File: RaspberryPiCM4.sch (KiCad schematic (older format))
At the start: 12 parts, among them U11 Compute_Module_4_Connectors

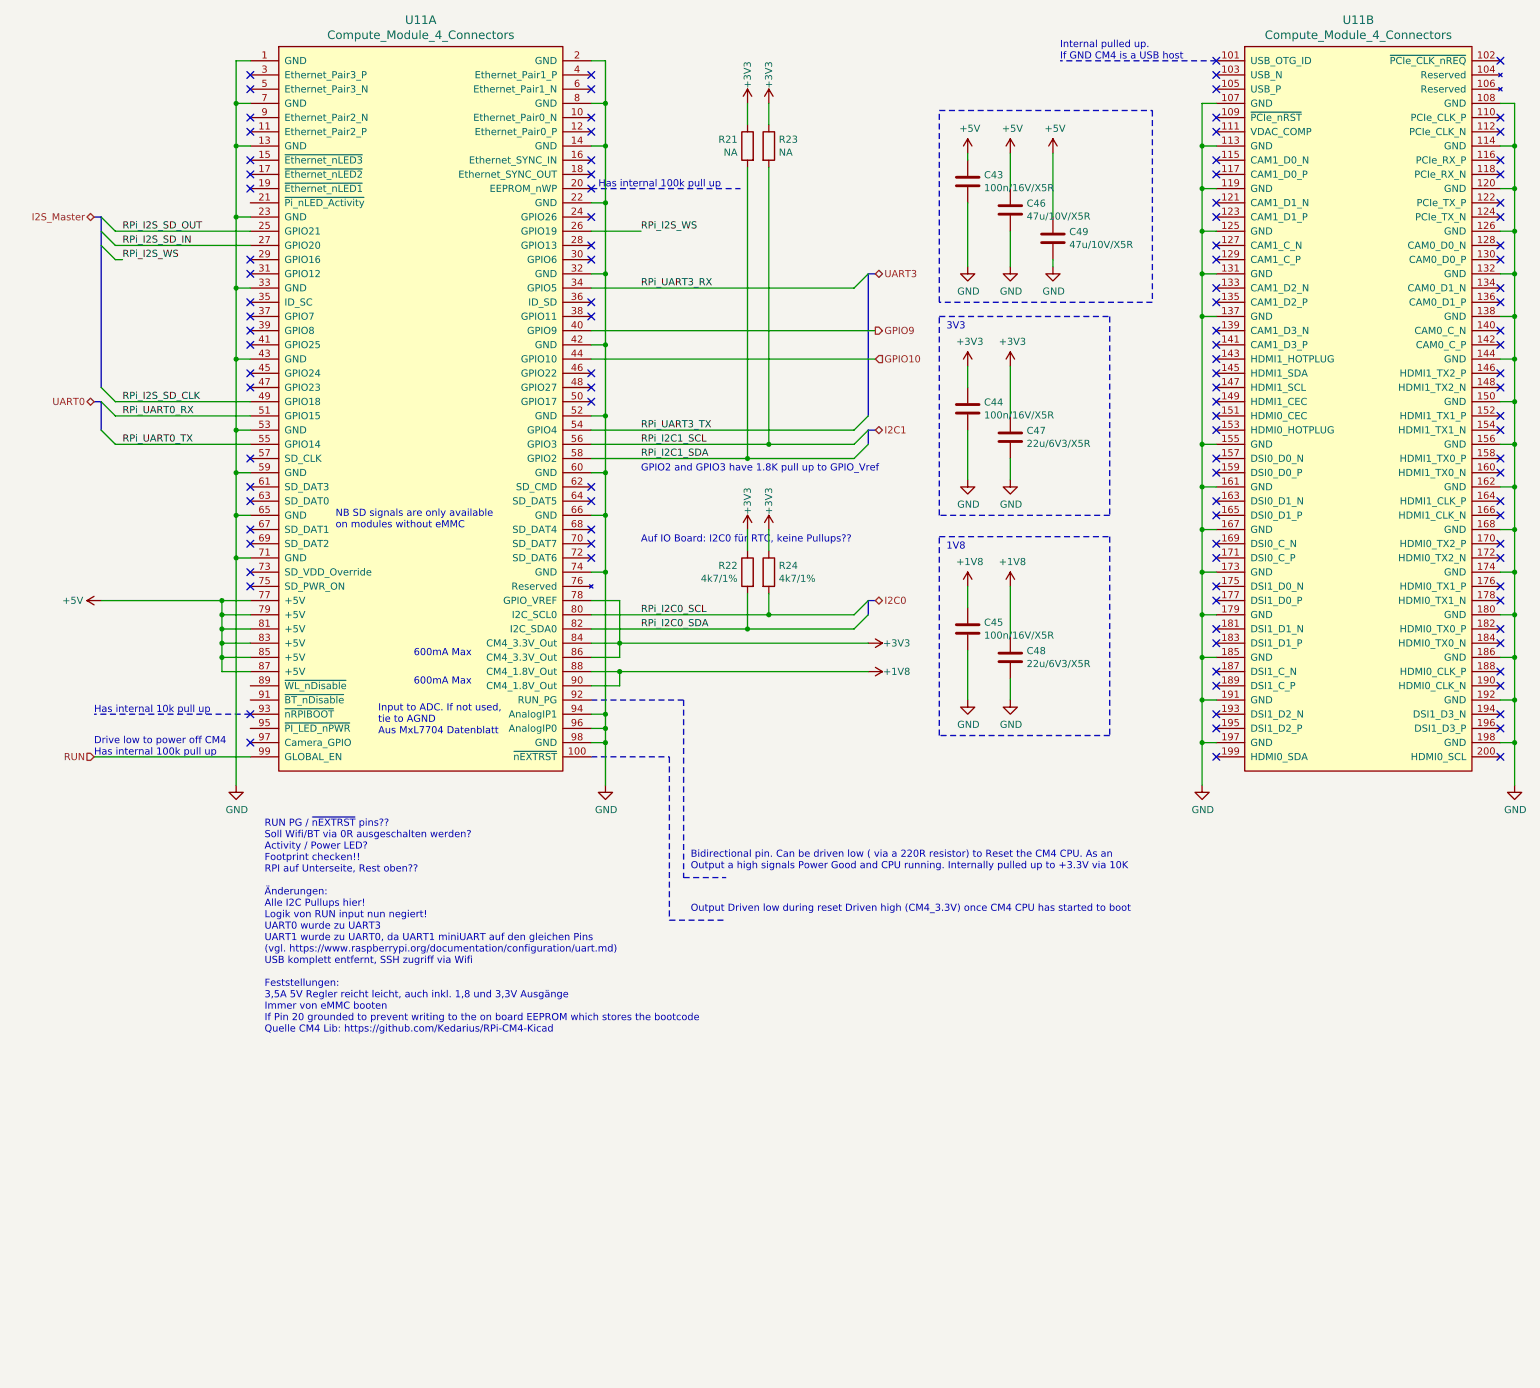
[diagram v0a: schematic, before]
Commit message: - 0R Bruecken hinzugefuegt - viele Detailinfos
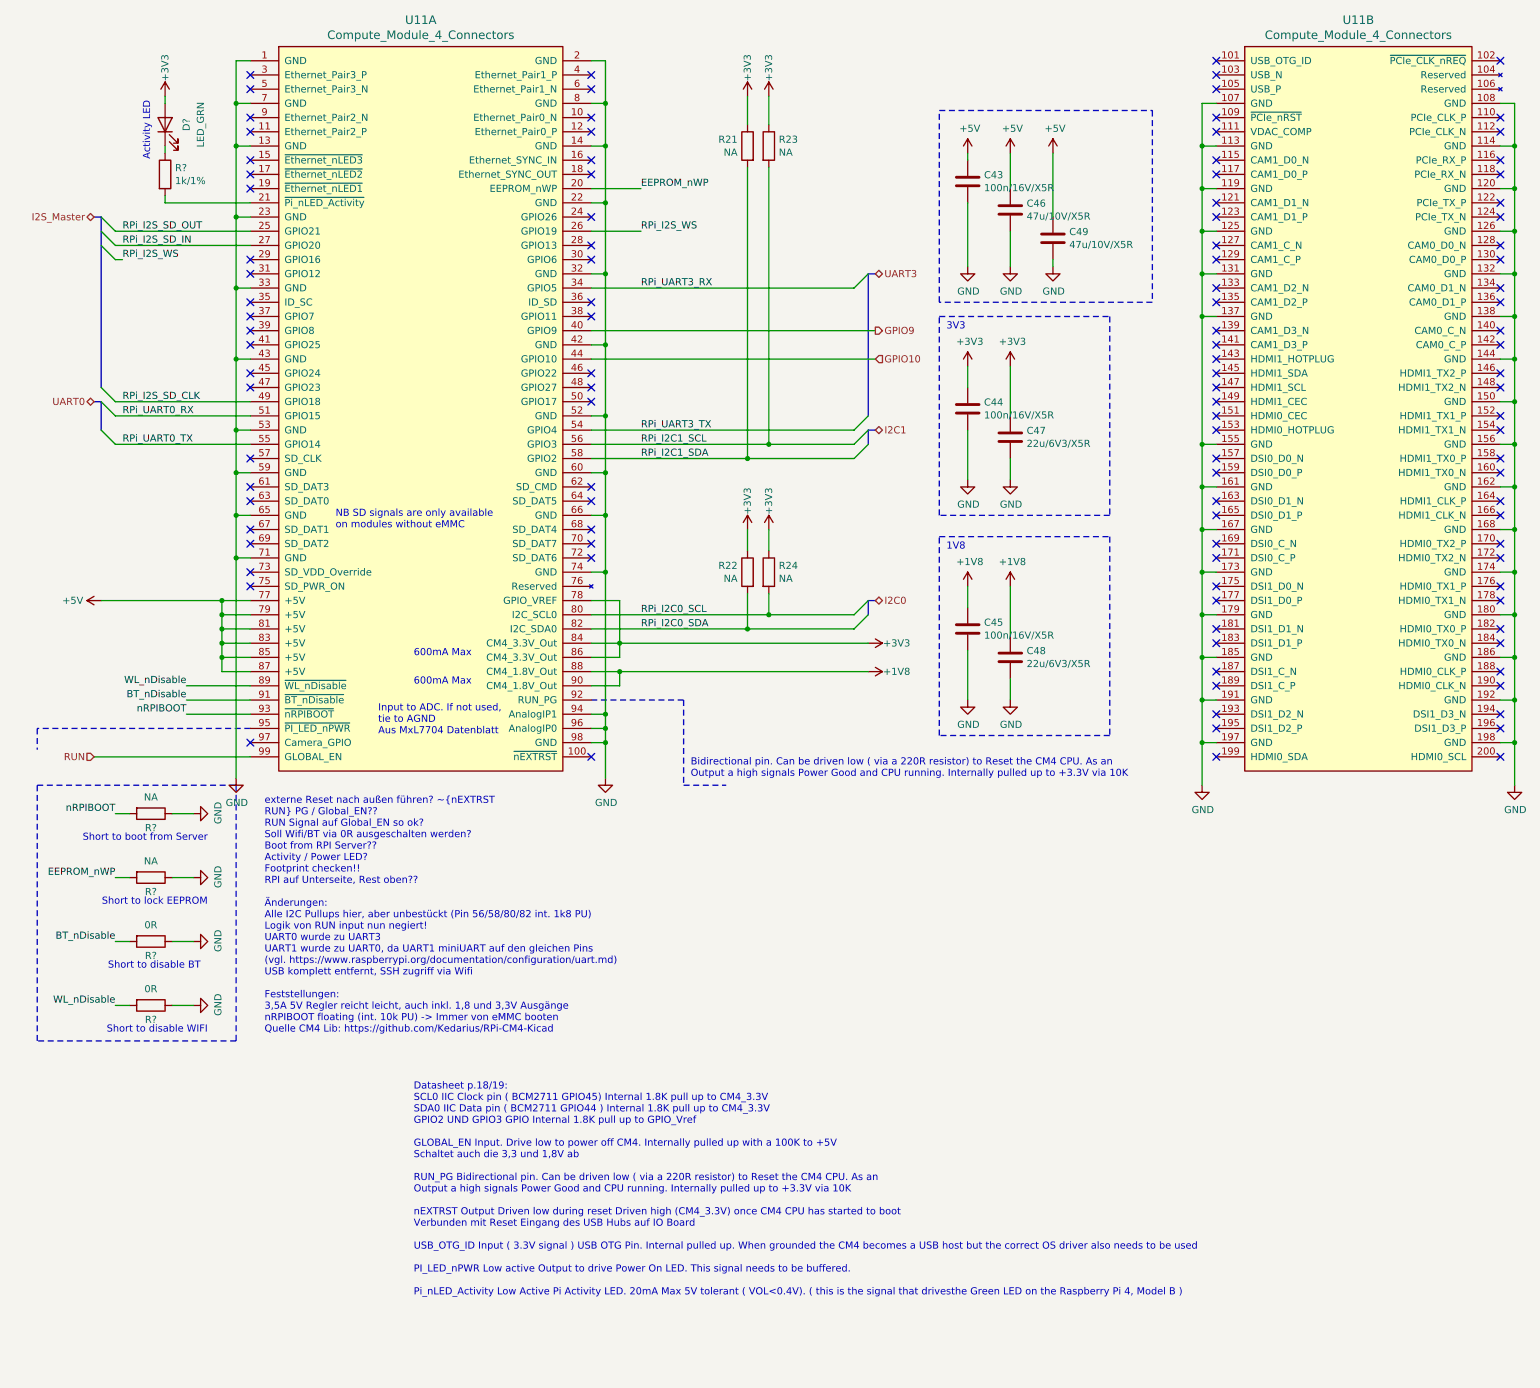
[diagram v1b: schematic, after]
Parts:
- added D?: LED_GRN, LED_SMD:LED_0603_1608Metric, symbol Device:LED
- added R? (x2): NA, Resistor_SMD:R_0402_1005Metric, symbol Device:R
- added R? (x2): 0R, Resistor_SMD:R_0402_1005Metric, symbol Device:R
- added R?: 1k/1%, Resistor_SMD:R_0603_1608Metric, symbol Device:R
- R21, R23: footprint Resistor_SMD:R_0603_1608Metric -> Resistor_SMD:R_0402_1005Metric
- R22, R24: value 4k7/1% -> NA; footprint Resistor_SMD:R_0603_1608Metric -> Resistor_SMD:R_0402_1005Metric
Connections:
- net +3V3: now also D?.2 (A)
- net GND: now also R?.1, R?.1, R?.1, R?.1
- net EEPROM_nWP: now reaches U11.20 (EEPROM_nWP)
- net EEPROM_nWP: now also R?.2
- net at U11.21 (~Pi_nLED_Activity): now also R?.2
- net WL_nDisable: now reaches U11.89 (~WL_nDisable)
- net WL_nDisable: now also R?.2
- net BT_nDisable: now reaches U11.91 (~BT_nDisable)
- net BT_nDisable: now also R?.2
- net nRPIBOOT: now reaches U11.93 (~nRPIBOOT)
- net nRPIBOOT: now also R?.2
- new net: D?.1 (K), R?.1
- no-connect marks 112 -> 111
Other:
- note added: "Activity LED"
- note added: "Datasheet p.18/19:\nSCL0 IIC Clock pin ( BCM2711 GPIO45) Internal 1.8K pull up to CM4_3.3V\nSDA0 IIC Data pin ( BCM2711 GPIO44 ) Internal 1.8K pull up to CM4_3.3V\nGPIO2 UND GPIO3 GPIO Internal 1.8K pull up to GPIO_Vref\n\nGLOBAL_EN Input. Drive low to power off CM4. Internally pulled up with a 100K to +5V\nSchaltet auch die 3,3 und 1,8V ab\n\nRUN_PG Bidirectional pin. Can be driven low ( via a 2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"
- note added: "Short to boot from Server"
- note added: "Short to disable BT"
- note added: "Short to disable WIFI"
- note added: "Short to lock EEPROM"
- note added: "externe Reset nach außen führen? ~nEXTRST\nRUN PG / Global_EN??\nRUN Signal auf Global_EN so ok?\nSoll Wifi/BT via 0R ausgeschalten werden?\nBoot from RPI Server??\nActivity / Power LED?\nFootprint checken!!\nRPI auf Unterseite, Rest oben??\n\nÄnderungen: \nAlle I2C Pullups hier, aber unbestückt (Pin 56/58/80/82 int. 1k8 PU)\nLogik von RUN input nun negiert!\nUART0 wurde zu UART3\nUART1 wurde zu 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"
- note removed: "Auf IO Board: I2C0 für RTC, keine Pullups??"
- note removed: "Drive low to power off CM4\nHas internal 100k pull up"
- note removed: "GPIO2 and GPIO3 have 1.8K pull up to GPIO_Vref"
- note removed: "Has internal 100k pull up"
- note removed: "Has internal 10k pull up"
- note removed: "Internal pulled up. \nIf GND CM4 is a USB host"
- note removed: "Output Driven low during reset Driven high (CM4_3.3V) once CM4 CPU has started to boot"
- note removed: "RUN PG / ~nEXTRST pins??\nSoll Wifi/BT via 0R ausgeschalten werden?\nActivity / Power LED?\nFootprint checken!!\nRPI auf Unterseite, Rest oben??\n\nÄnderungen: \nAlle I2C Pullups hier!\nLogik von RUN input nun negiert!\nUART0 wurde zu UART3\nUART1 wurde zu UART0, da UART1 miniUART auf den gleichen Pins\n(vgl. https://www.raspberrypi.org/documentation/configuration/uart.md)\nUSB komplett entfernt,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"

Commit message: - Bus Topologie entfernt - Levelshifter auf eigenes Blatt, abgeschlossen
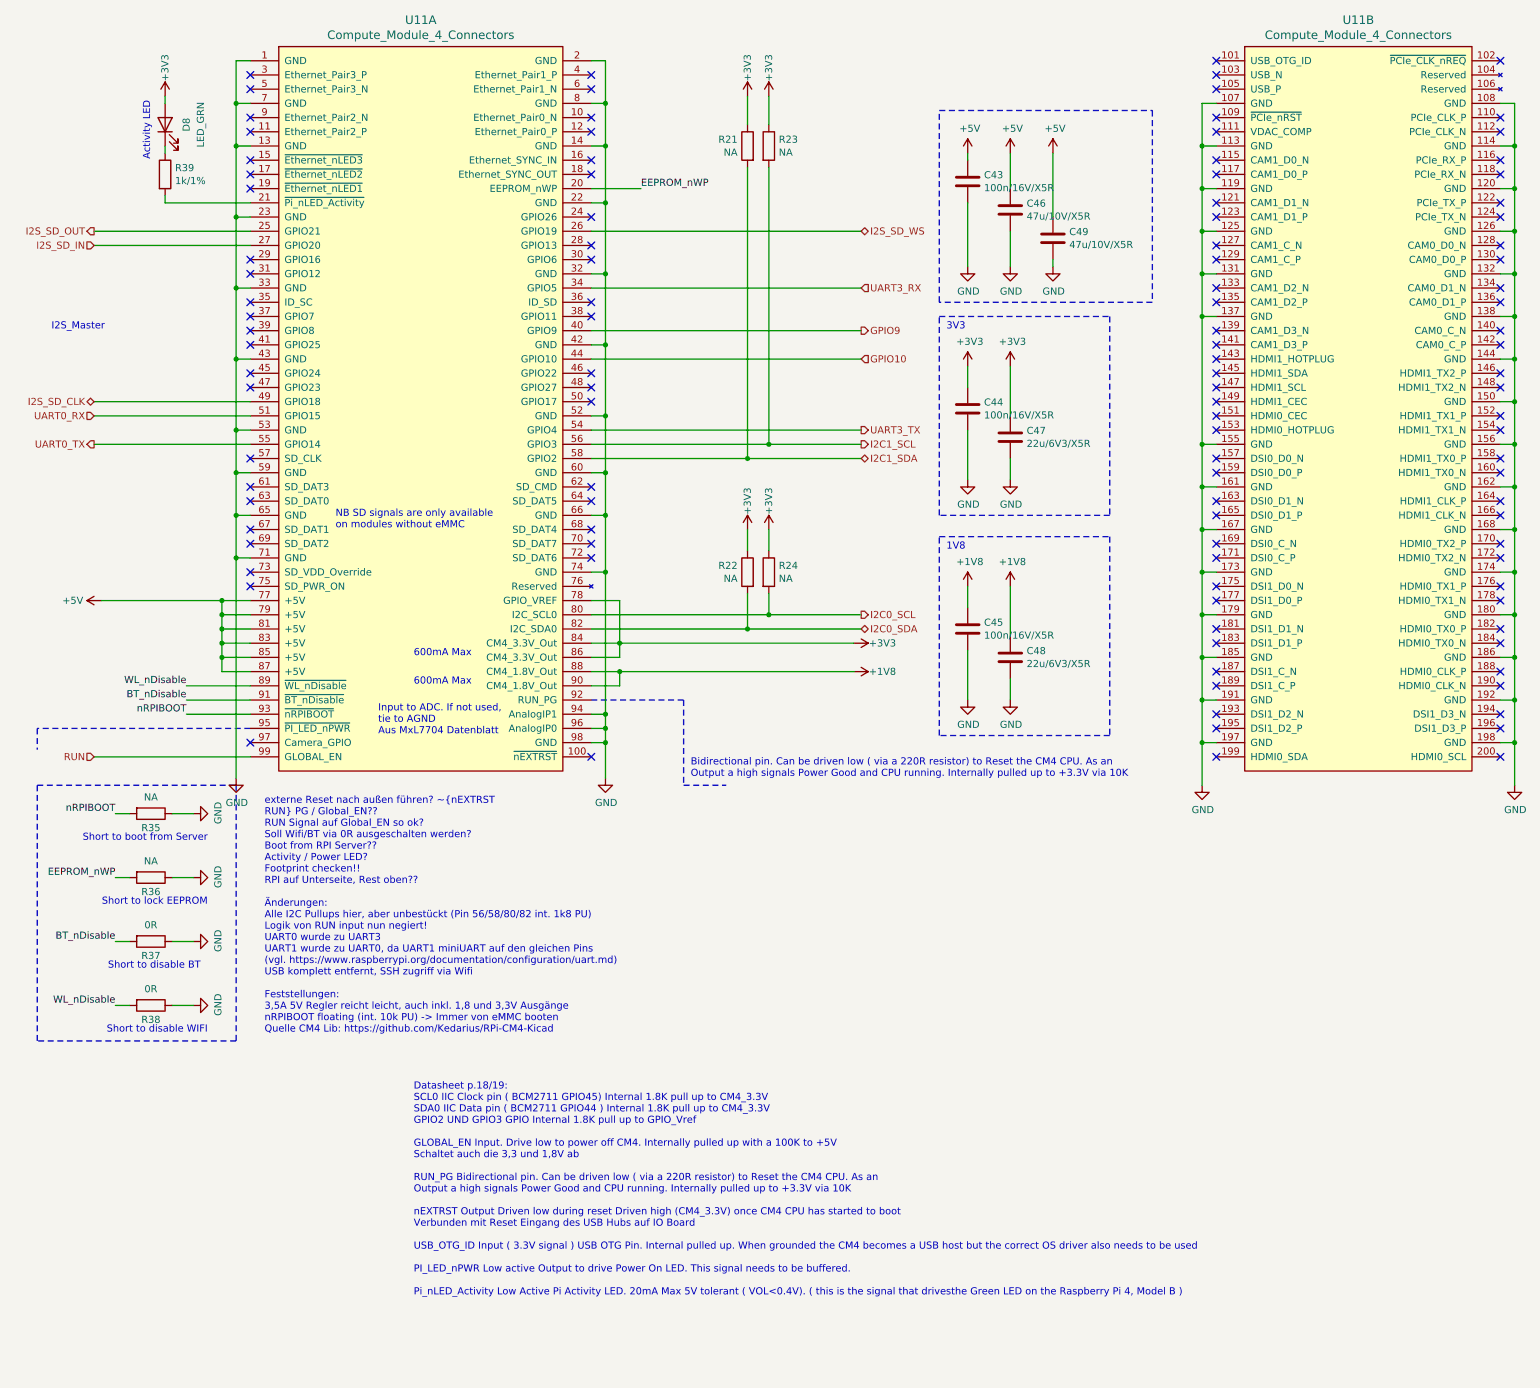
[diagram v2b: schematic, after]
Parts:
- gave numbers to parts that had none: 6
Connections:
- net RPi_I2C0_SCL renamed I2C0_SCL
- net RPi_I2C0_SDA renamed I2C0_SDA
- net RPi_I2C1_SCL renamed I2C1_SCL
- net RPi_I2C1_SDA renamed I2C1_SDA
- net RPi_I2S_SD_CLK renamed I2S_SD_CLK
- net RPi_I2S_SD_IN renamed I2S_SD_IN
- net RPi_I2S_SD_OUT renamed I2S_SD_OUT
- net RPi_I2S_WS renamed I2S_SD_WS
- net RPi_UART0_RX renamed UART0_RX
- net RPi_UART0_TX renamed UART0_TX
- net RPi_UART3_RX renamed UART3_RX
- net RPi_UART3_TX renamed UART3_TX
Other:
- note added: "I2S_Master"

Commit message: - CM4 update - Todo Liste auf Hauptschaltplan hinzugefügt
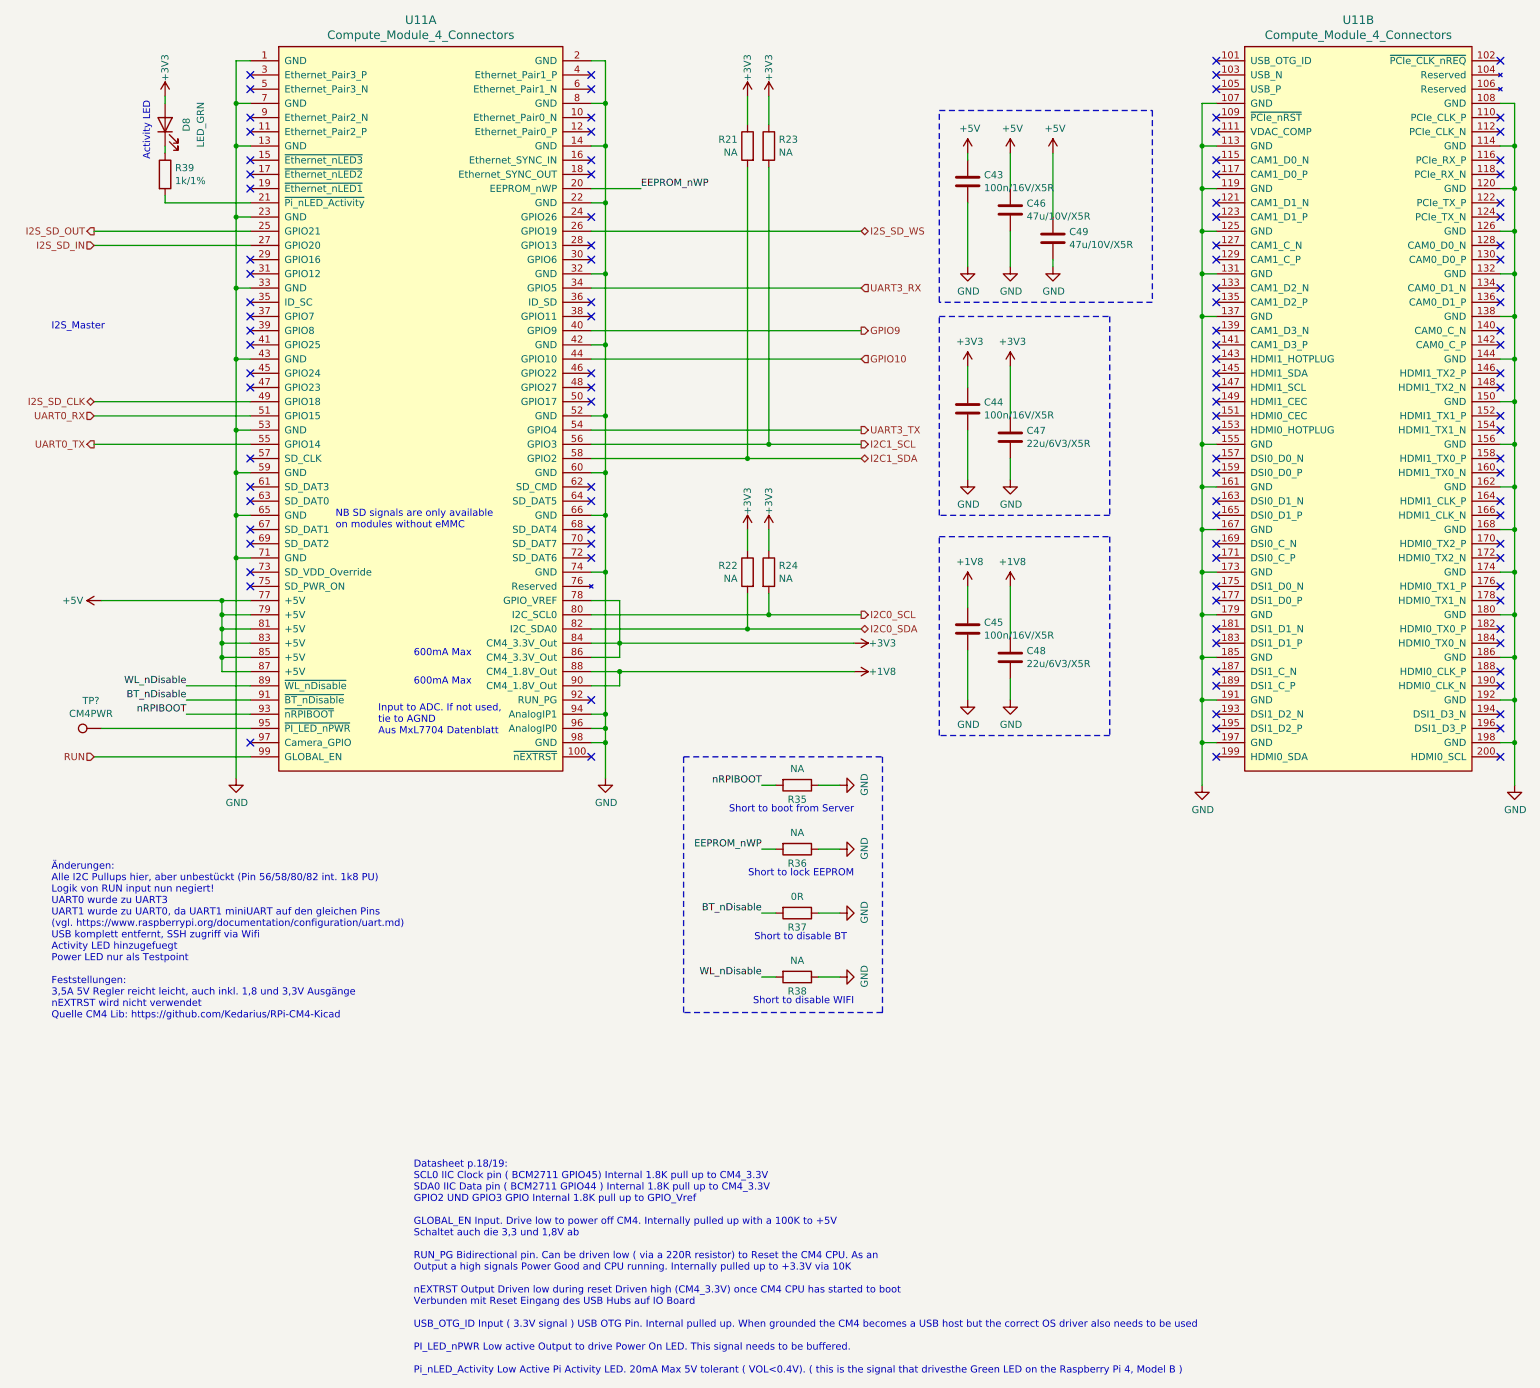
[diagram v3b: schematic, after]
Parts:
- added TP?: CM4PWR, TestPoint:TestPoint_Pad_D1.5mm, symbol Connector:TestPoint
- R38: value 0R -> NA
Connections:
- net at U11.95 (~PI_LED_nPWR): now also TP?.1
- no-connect marks 111 -> 112
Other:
- note added: "Änderungen: \nAlle I2C Pullups hier, aber unbestückt (Pin 56/58/80/82 int. 1k8 PU)\nLogik von RUN input nun negiert!\nUART0 wurde zu UART3\nUART1 wurde zu UART0, da UART1 miniUART auf den gleichen Pins\n(vgl. https://www.raspberrypi.org/documentation/configuration/uart.md)\nUSB komplett entfernt, SSH zugriff via Wifi\nActivity LED hinzugefuegt\nPower LED nur als Testpoint\n\nFeststellungen: \n3,5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"
- note removed: "1V8"
- note removed: "3V3"
- note removed: "Bidirectional pin. Can be driven low ( via a 220R resistor) to Reset the CM4 CPU. As an\nOutput a high signals Power Good and CPU running. Internally pulled up to +3.3V via 10K"
- note removed: "externe Reset nach außen führen? ~nEXTRST\nRUN PG / Global_EN??\nRUN Signal auf Global_EN so ok?\nSoll Wifi/BT via 0R ausgeschalten werden?\nBoot from RPI Server??\nActivity / Power LED?\nFootprint checken!!\nRPI auf Unterseite, Rest oben??\n\nÄnderungen: \nAlle I2C Pullups hier, aber unbestückt (Pin 56/58/80/82 int. 1k8 PU)\nLogik von RUN input nun negiert!\nUART0 wurde zu UART3\nUART1 wurde zu 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"
- moved on the sheet: R35, R36, R37, R38
